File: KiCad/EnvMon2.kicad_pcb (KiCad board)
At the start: 2 copper layers, 58 x 37 mm, 32 parts, among them J1 USB-C, J2 DC, J3 TEMP, M1 OLED1.5-RGB, U1 LMR16006+FB, U2 SCD41, U3 FT231XQ, U4 ESP32-PICO-MINI-02, U5 QR

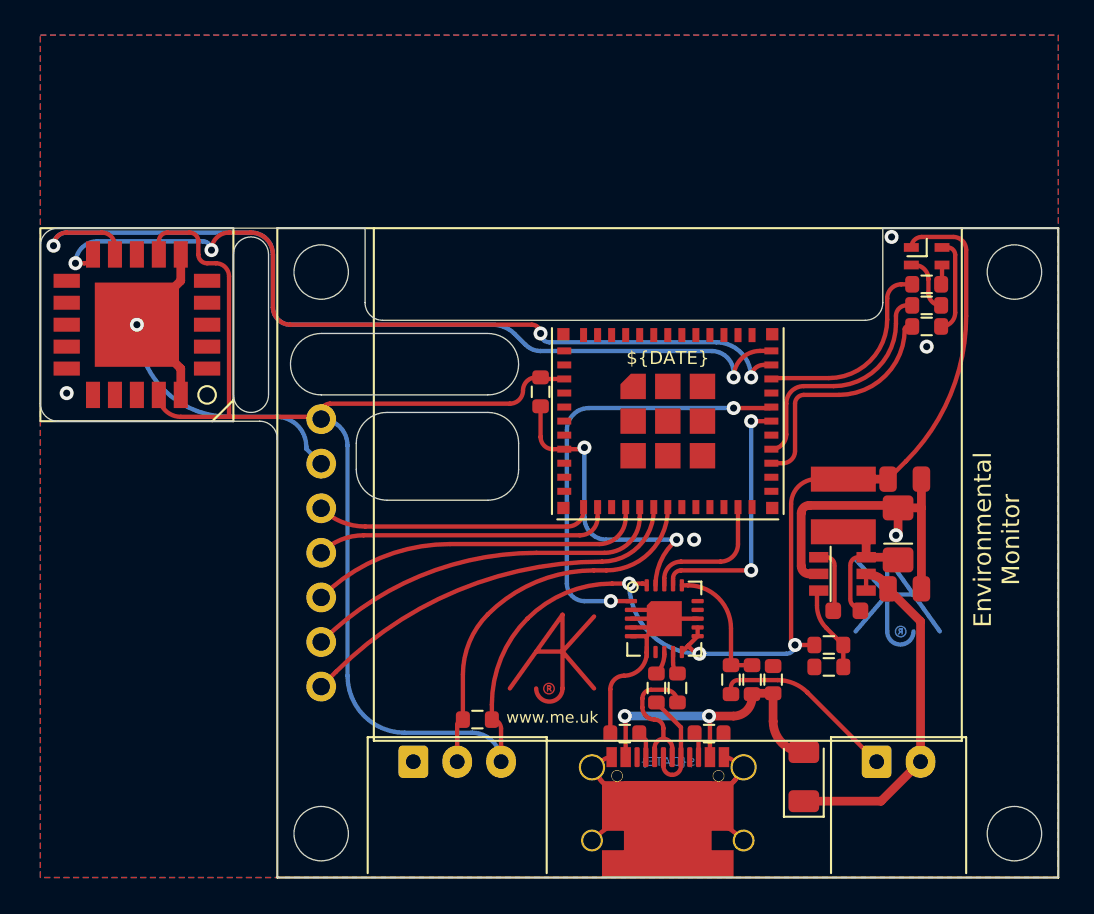
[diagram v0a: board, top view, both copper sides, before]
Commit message: Changed artwork for clearances
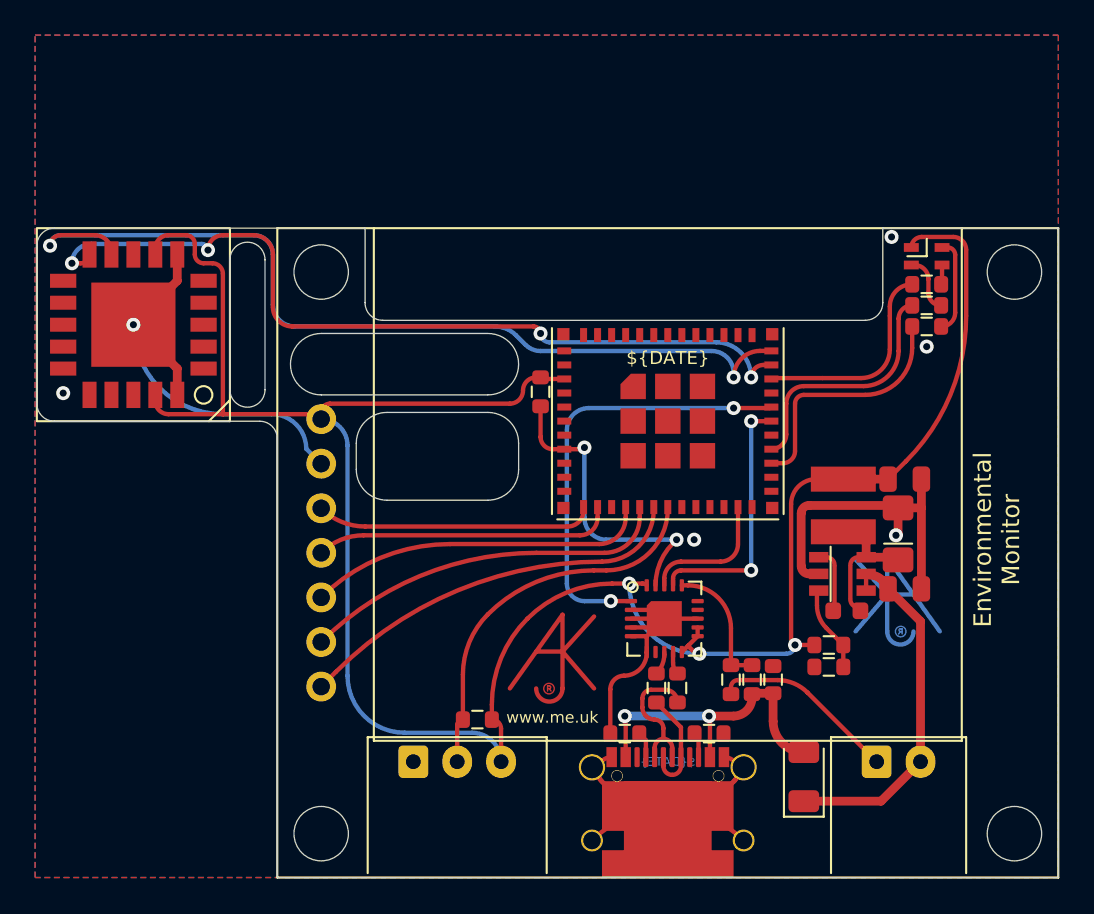
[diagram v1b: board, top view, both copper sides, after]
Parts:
- moved U2 0.20 mm to (91.8, 68.5)
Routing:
- net B: track 13.4 -> 14.1 mm
- net G: track 11.4 -> 12.0 mm
- net R: track 13.4 -> 14.0 mm
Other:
- board size 58 x 37 mm -> 58.2 x 37 mm

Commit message: DRC tweak
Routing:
- net GND: vias 6 -> 5
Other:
- rule pad_to_mask_clearance: 0 -> 0.01

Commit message: Resitors
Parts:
- R1: value 10M 1% or 0R -> 100k 1% or 0R
- R2: value 3M 1% or NF -> 30k 1% or NF
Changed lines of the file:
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@@
       (effects (font (size 0.5 0.5) (thickness 0.08)))
     )
-    (fp_text value "10M 1% or 0R" (at 0 0) (layer "F.Fab")
+    (fp_text value "100k 1% or 0R" (at 0 0) (layer "F.Fab")
       (effects (font (size 0.4 0.4) (thickness 0.08)))
     )
@@
       (effects (font (size 0.5 0.5) (thickness 0.08)))
     )
-    (fp_text value "3M 1% or NF" (at 0 0) (layer "F.Fab")
+    (fp_text value "30k 1% or NF" (at 0 0) (layer "F.Fab")
       (effects (font (size 0.4 0.4) (thickness 0.08)))
     )

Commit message: Tidy
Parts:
- D2: footprint Diode_SMD:D_1206_3216Metric -> RevK:D_1206

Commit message: Tweatk
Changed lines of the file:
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@@
   (gr_line (start 144.5 100) (end 144.5 63) (layer "Eco1.User") (width 0.1))
   (gr_line (start 86.3 63) (end 86.3 74) (layer "Eco1.User") (width 0.1))
+  (gr_line (start 144.5 100) (end 100 100) (layer "Eco2.User") (width 0.1))
   (gr_line (start 100 100) (end 100 63) (layer "Eco2.User") (width 0.1))
   (gr_line (start 144.5 63) (end 144.5 100) (layer "Eco2.User") (width 0.1))
   (gr_line (start 100 63) (end 144.5 63) (layer "Eco2.User") (width 0.1))
-  (gr_line (start 144.5 100) (end 100 100) (layer "Eco2.User") (width 0.1))
   (gr_line (start 99 74) (end 87.3 74) (layer "Edge.Cuts") (width 0.05))
   (gr_arc (start 97.3 64.8) (mid 98.3 63.8) (end 99.3 64.8) (layer "Edge.Cuts") (width 0.05))
@@
   (arc (start 115.7 75.59325) (mid 115.205025 75.388225) (end 115 74.89325) (width 0.25) (layer "F.Cu") (net 43))
   (arc (start 117.40675 75.59325) (mid 117.472688 75.565938) (end 117.5 75.5) (width 0.25) (layer "F.Cu") (net 43))
-  (segment (start 122.75 80.75) (end 118.75 80.75) (width 0.25) (layer "B.Cu") (net 43))
-  (segment (start 117.5 79.5) (end 117.5 75.5) (width 0.25) (layer "B.Cu") (net 43))
-  (arc (start 118.75 80.75) (mid 117.866117 80.383883) (end 117.5 79.5) (width 0.25) (layer "B.Cu") (net 43))
+  (segment (start 117.5 75.5) (end 121.22 75.5) (width 0.25) (layer "B.Cu") (net 43))
+  (segment (start 122.75 80.75) (end 122.75 77.03) (width 0.25) (layer "B.Cu") (net 43))
+  (arc (start 122.75 77.03) (mid 122.301873 75.948127) (end 121.22 75.5) (width 0.25) (layer "B.Cu") (net 43))
   (segment (start 136.125 65.1) (end 136.3 65.1) (width 0.25) (layer "F.Cu") (net 44))
   (segment (start 137.825 67.4) (end 137.808217 67.4) (width 0.25) (layer "F.Cu") (net 44))

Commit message: Tidy
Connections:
- net OLED-CS0 renamed OLED-CS
- net OLED-SCLK renamed OLED-SCK
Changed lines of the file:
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@@
   (net 13 "OLED-RST")
   (net 14 "OLED-DC")
-  (net 15 "OLED-CS0")
-  (net 16 "OLED-SCLK")
+  (net 15 "OLED-SCK")
+  (net 16 "OLED-CS")
   (net 17 "OLED-MOSI")
   (net 18 "CO2-SDA")
@@
       (net 17 "OLED-MOSI") (pinfunction "DIN") (pintype "input"))
     (pad "4" thru_hole circle (at 42 -18.5 180) (size 1.7 1.7) (drill 1) (layers *.Cu *.Mask)
-      (net 16 "OLED-SCLK") (pinfunction "CLK") (pintype "input"))
+      (net 15 "OLED-SCK") (pinfunction "CLK") (pintype "input"))
     (pad "5" thru_hole circle (at 42 -21.04 180) (size 1.7 1.7) (drill 1) (layers *.Cu *.Mask)
-      (net 15 "OLED-CS0") (pinfunction "CS") (pintype "input"))
+      (net 16 "OLED-CS") (pinfunction "CS") (pintype "input"))
     (pad "6" thru_hole circle (at 42 -23.58 180) (size 1.7 1.7) (drill 1) (layers *.Cu *.Mask)
       (net 14 "OLED-DC") (pinfunction "DC") (pintype "input"))
@@
       (net 17 "OLED-MOSI") (pinfunction "IO32") (pintype "bidirectional"))
     (pad "13" smd rect (at -4 4.9) (size 0.4 0.8) (layers "F.Cu" "F.Paste" "F.Mask")
-      (net 16 "OLED-SCLK") (pinfunction "IO33") (pintype "bidirectional"))
+      (net 15 "OLED-SCK") (pinfunction "IO33") (pintype "bidirectional"))
     (pad "14" smd rect (at -3.2 4.9) (size 0.4 0.8) (layers "F.Cu" "F.Paste" "F.Mask")
       (net 11 "GND") (pinfunction "GND") (pintype "power_in"))
     (pad "15" smd rect (at -2.4 4.9) (size 0.4 0.8) (layers "F.Cu" "F.Paste" "F.Mask")
-      (net 15 "OLED-CS0") (pinfunction "IO25") (pintype "bidirectional"))
+      (net 16 "OLED-CS") (pinfunction "IO25") (pintype "bidirectional"))
     (pad "16" smd rect (at -1.6 4.9) (size 0.4 0.8) (layers "F.Cu" "F.Paste" "F.Mask")
       (net 14 "OLED-DC") (pinfunction "IO26") (pintype "bidirectional"))
@@
   (arc (start 114.764204 81.5) (mid 108.126865 82.820249) (end 102.5 86.58) (width 0.25) (layer "F.Cu") (net 14))
   (arc (start 120.65 79.49325) (mid 120.062237 80.912237) (end 118.64325 81.5) (width 0.25) (layer "F.Cu") (net 14))
-  (segment (start 119.85 78.84325) (end 119.85 79.49325) (width 0.25) (layer "F.Cu") (net 15))
-  (segment (start 118.34325 81) (end 109.839209 81) (width 0.25) (layer "F.Cu") (net 15))
-  (arc (start 119.85 79.49325) (mid 119.408683 80.558683) (end 118.34325 81) (width 0.25) (layer "F.Cu") (net 15))
-  (arc (start 109.839209 81) (mid 105.867258 81.79007) (end 102.5 84.04) (width 0.25) (layer "F.Cu") (net 15))
-  (segment (start 117.24325 80.5) (end 104.914213 80.5) (width 0.25) (layer "F.Cu") (net 16))
-  (segment (start 118.25 78.84325) (end 118.25 79.49325) (width 0.25) (layer "F.Cu") (net 16))
-  (arc (start 118.25 79.49325) (mid 117.95513 80.20513) (end 117.24325 80.5) (width 0.25) (layer "F.Cu") (net 16))
-  (arc (start 104.914213 80.5) (mid 103.607651 80.759891) (end 102.5 81.5) (width 0.25) (layer "F.Cu") (net 16))
+  (segment (start 117.24325 80.5) (end 104.914213 80.5) (width 0.25) (layer "F.Cu") (net 15))
+  (segment (start 118.25 78.84325) (end 118.25 79.49325) (width 0.25) (layer "F.Cu") (net 15))
+  (arc (start 118.25 79.49325) (mid 117.95513 80.20513) (end 117.24325 80.5) (width 0.25) (layer "F.Cu") (net 15))
+  (arc (start 104.914213 80.5) (mid 103.607651 80.759891) (end 102.5 81.5) (width 0.25) (layer "F.Cu") (net 15))
+  (segment (start 119.85 78.84325) (end 119.85 79.49325) (width 0.25) (layer "F.Cu") (net 16))
+  (segment (start 118.34325 81) (end 109.839209 81) (width 0.25) (layer "F.Cu") (net 16))
+  (arc (start 119.85 79.49325) (mid 119.408683 80.558683) (end 118.34325 81) (width 0.25) (layer "F.Cu") (net 16))
+  (arc (start 109.839209 81) (mid 105.867258 81.79007) (end 102.5 84.04) (width 0.25) (layer "F.Cu") (net 16))
   (segment (start 116.54325 80) (end 116.49325 80) (width 0.25) (layer "F.Cu") (net 17))
   (segment (start 117.45 78.89325) (end 117.45 79.09325) (width 0.25) (layer "F.Cu") (net 17))

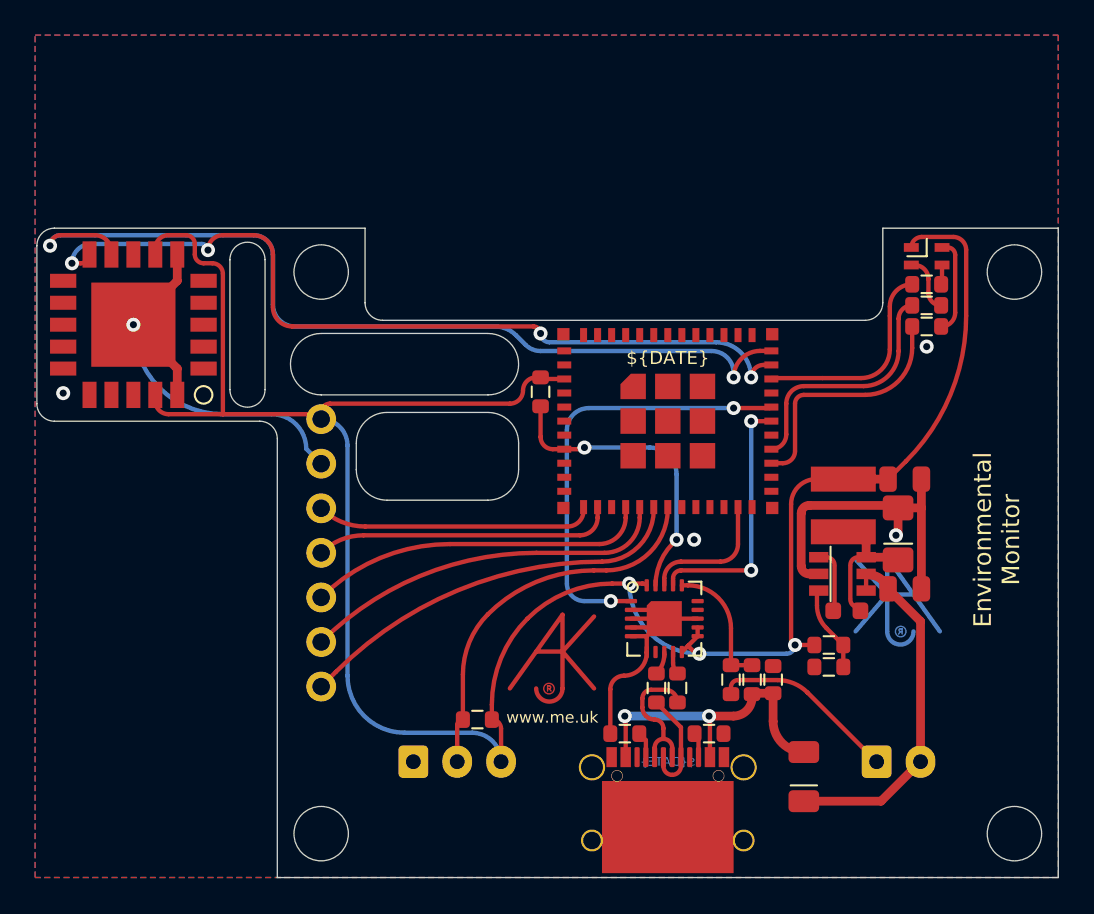
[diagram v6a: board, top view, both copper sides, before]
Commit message: Change to M2 screws
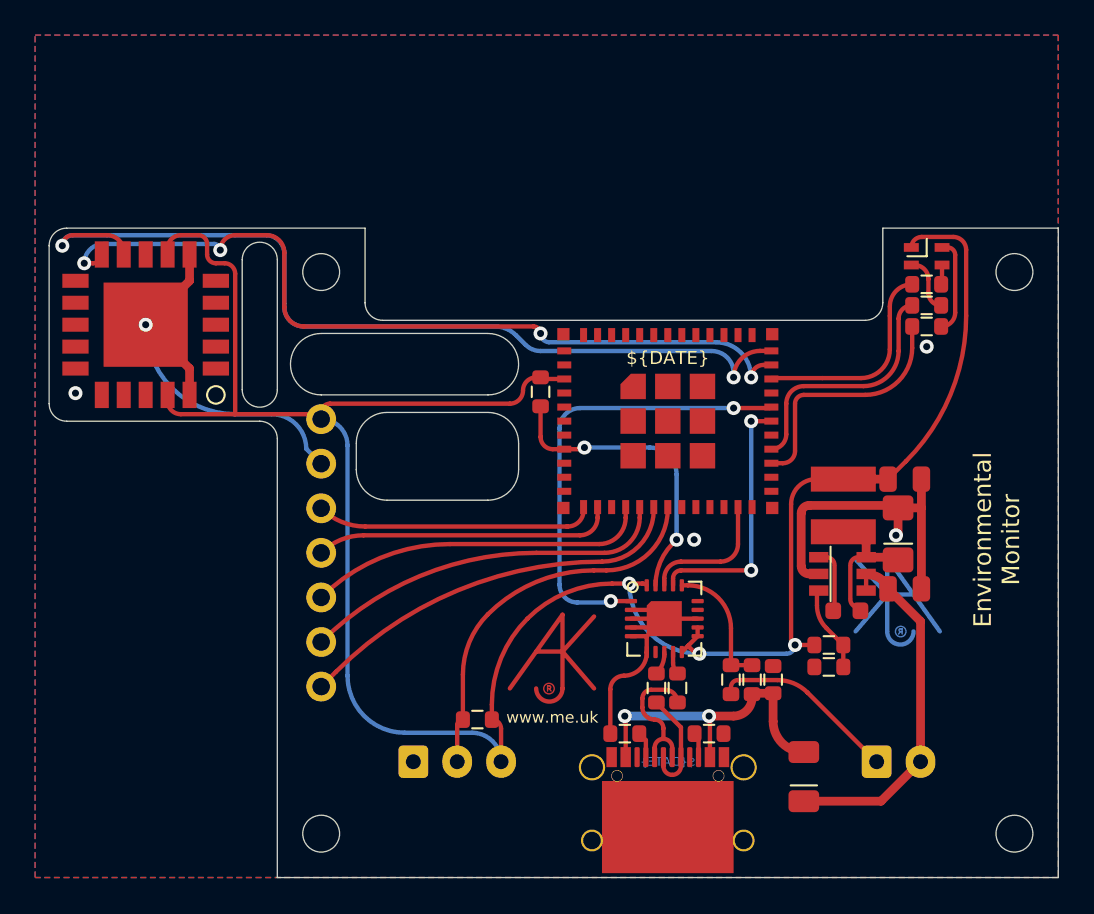
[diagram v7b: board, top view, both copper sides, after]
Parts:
- moved U2 0.70 mm to (92.5, 68.5)
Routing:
- net O: track 25.3 -> 26.3 mm
- net GND: track 50.1 -> 49.4 mm
- net +3V3: track 128.4 -> 127.7 mm
- net CO2-SDA: track 48.4 -> 47.8 mm
- net CO2-SCL: track 52.1 -> 51.5 mm
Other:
- board size 58.2 x 37 mm -> 57.5 x 37 mm

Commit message: Buttons
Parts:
- added SW1: SW_Push, Button_Switch_THT:SW_PUSH_6mm_H13mm, F.Cu at (89.2, 78.2)
- added SW2: SW_Push, Button_Switch_THT:SW_PUSH_6mm_H13mm, F.Cu at (89.2, 85.8)
- added SW3: SW_Push, Button_Switch_THT:SW_PUSH_6mm_H13mm, F.Cu at (89.3, 93.2)
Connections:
- U4 pad 5: unconnected-(U4-Pad5) -> BUTTON1
- U4 pad 6: unconnected-(U4-Pad6) -> BUTTON2
- U4 pad 7: unconnected-(U4-Pad7) -> BUTTON3
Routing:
- net BUTTON2: track 0.00 -> 53.6 mm, vias 0 -> 1
- net BUTTON3: track 0.00 -> 46.0 mm, vias 0 -> 1
- net BUTTON1: track 0.00 -> 36.6 mm, vias 0 -> 1
- net O: track 26.3 -> 19.7 mm
- net +3V3: track 127.7 -> 130.2 mm, vias 3 -> 4
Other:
- outline, holes or cut-outs redrawn
- board text added: "37"
- board text added: "38"
- board text added: "39"
